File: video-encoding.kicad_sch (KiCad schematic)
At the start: 48 parts, among them J2 DIN8, Q1 2N2222, U10 LM318, U11 LM318, U12 LM318, U13 LM1881, U14 LM318, U15 LM318, U16 LM318, U8 4066, U9 LM318

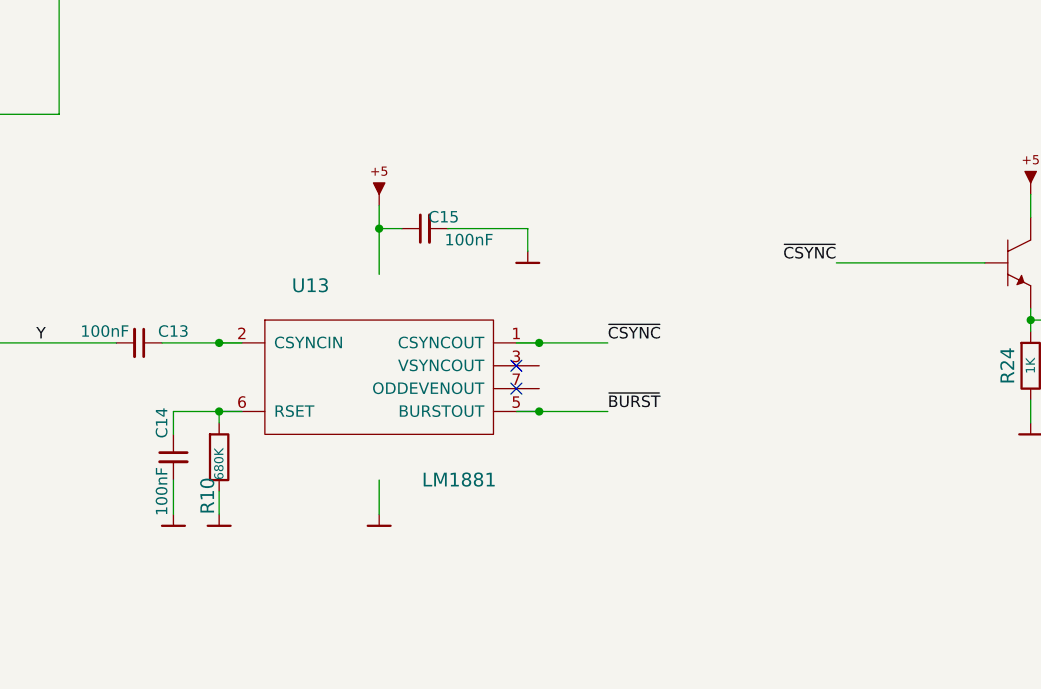
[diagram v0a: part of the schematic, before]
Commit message: Update to latest Artemisa kicadlibs
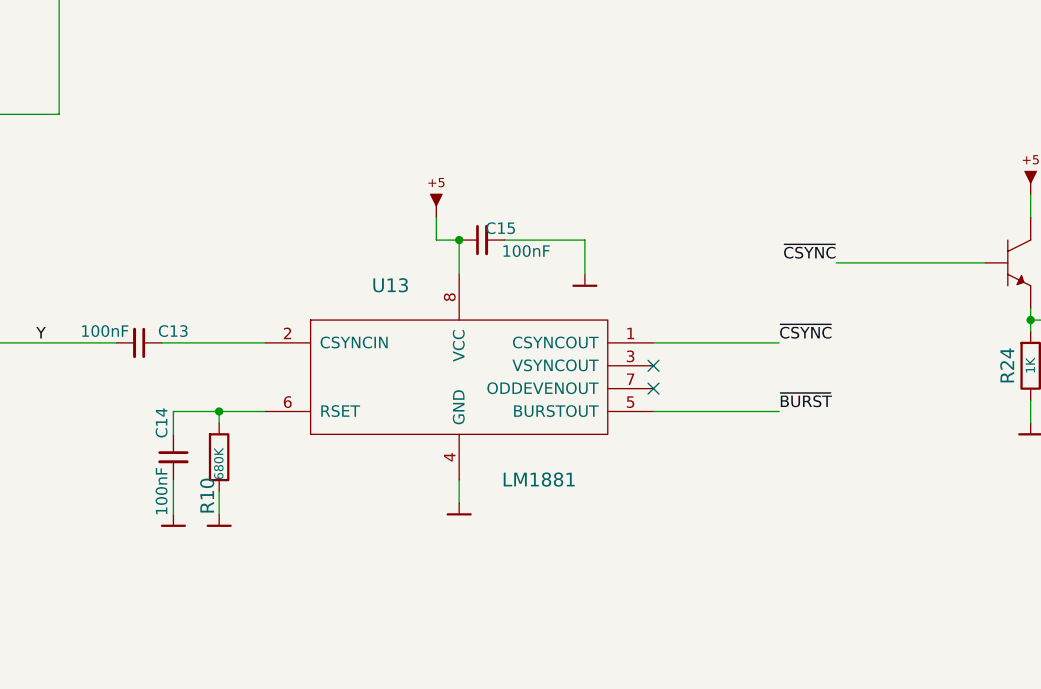
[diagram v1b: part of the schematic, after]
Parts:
- U13: symbol artemisa:LM1881 -> PCM_artemisa:LM1881
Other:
- moved on the sheet: C15

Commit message: Replace LM318 by MCP6284
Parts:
- removed U10, U11, U12, U14, U15, U16, U9: LM318, symbol artemisa:LM318
- added U17, U18: MCP6284, symbol PCM_artemisa:MCP6284
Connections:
- net B: now also U18.7 (OUT)
- net B_Y: now also U17.12 (IN+)
- net B_Y': now also U17.14 (OUT)
- net G: now also U18.8 (OUT)
- net GND: now also U17.11 (V-), U18.11 (V-), U18.12 (IN+)
- net R: now also U18.1 (OUT)
- net R_Y: now also U17.10 (IN+)
- net R_Y': now also U17.8 (OUT)
- net VCC: now also U17.4 (V+), U18.4 (V+)
- net VREF: now also U17.1 (OUT), U17.2 (IN-)
- net Y: now also U17.5 (IN+)
- net Y': now also U17.7 (OUT)
- net at R22.2, R25.2: now also U18.2 (IN-)
- net at R18.1, R19.1: now also U18.3 (IN+)
- net at R23.2, R26.2: now also U18.6 (IN-)
- net at R20.1, R21.1: now also U18.5 (IN+)
- net at R16.1, R17.1, R27.2: now also U18.9 (IN-)
- net at R14.1, R15.2: now also U18.10 (IN+)
- net at C12.1, U8.11: now also U17.3 (IN+)
- net at R11.2, R7.1: now also U17.6 (IN-)
- net at R12.2, R8.1: now also U17.9 (IN-)
- net at R13.2, R9.1: now also U17.13 (IN-)
- new net: U18.13 (IN-), U18.14 (OUT)
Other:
- note added: "Unit not used. Configured as voltage follower of GND."

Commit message: Use spare MCP6294 as CSYNC buffer
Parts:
- removed Q1: 2N2222, symbol artemisa:2N2222
- removed R24: 1K, symbol artemisa:R
- C10, C12, C15: footprint artemisa:Disc_capacitor -> PCM_artemisa:Disc_capacitor
- C13, C14: footprint (none) -> PCM_artemisa:Disc_capacitor
- J2: footprint (none) -> PCM_artemisa:DIN8
- R1, R10, R11, R12, R13, R14, R15, R16, R17, R18, R19, R2, R20, R21, R22, R23, R25, R26, R27, R28, R29, R3, R30, R31, R36, R4, R5, R6, R7, R8, R9: footprint (none) -> PCM_artemisa:Axial_resistor
- U17, U18: value MCP6284 -> MCP6294; footprint (none) -> PCM_artemisa:DIP-14_300; symbol PCM_artemisa:MCP6284 -> PCM_artemisa:MCP6294
- U8: footprint (none) -> PCM_artemisa:DIP-14_300
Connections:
- net GND: no longer U18.12 (IN+)
- net ~{CSYNC}: now also U18.12 (IN+)
- net at R36.1: now also U18.13 (IN-), U18.14 (OUT)
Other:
- note added: "CSYNC is buffered, as TV sets can drain more current than LM1881 can drive"
- note removed: "Unit not used. Configured as voltage follower of GND."
- moved on the sheet: C15, J2, R28, R29, R30, R31, R36, U18D
